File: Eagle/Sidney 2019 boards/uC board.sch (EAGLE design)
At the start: 55 parts, among them J1 39-28-1043

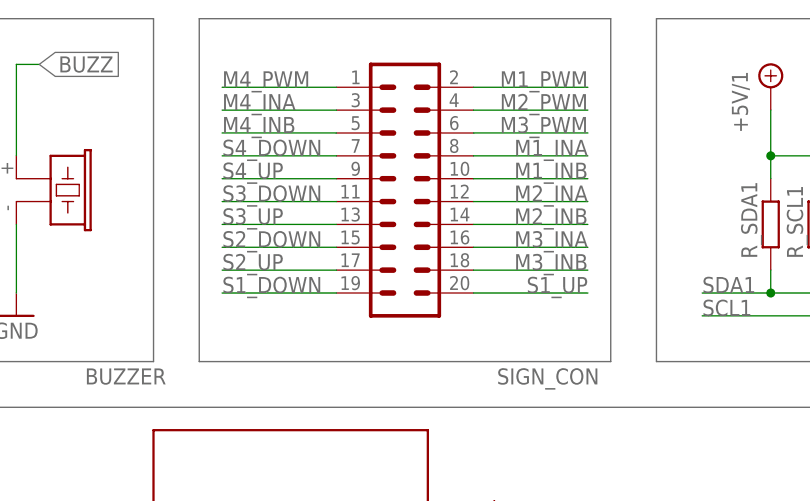
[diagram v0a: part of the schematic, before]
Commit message: Finished components lists for both boards and fixed line sensors' connectors pinout
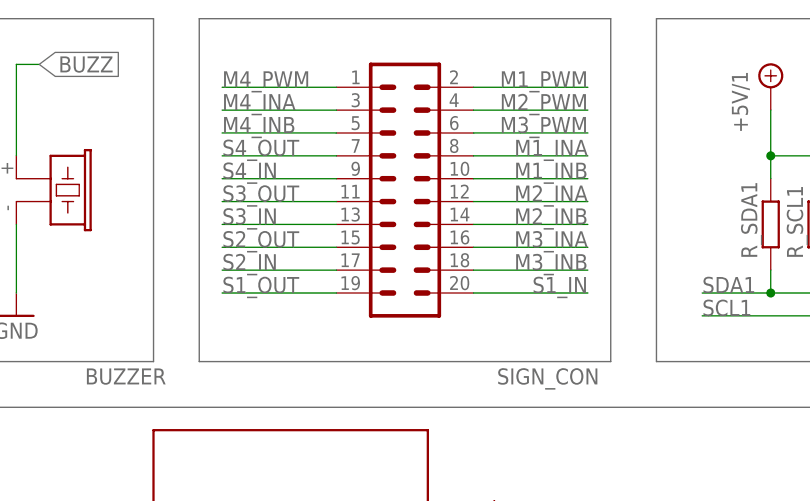
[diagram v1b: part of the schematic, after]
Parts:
- R_SW_DX, R_SW_SX: device rcl:R-EU_R0805 -> rcl:R-EU_R1206
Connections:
- new net S1_IN: SIGN_CON.20
- new net S1_OUT: SIGN_CON.19
- new net S2_IN: SIGN_CON.17
- new net S2_OUT: SIGN_CON.15
- new net S3_IN: SIGN_CON.13
- new net S3_OUT: SIGN_CON.11
- new net S4_IN: SIGN_CON.9
- new net S4_OUT: SIGN_CON.7
- net S1_DOWN: no longer SIGN_CON.19
- net S1_UP: no longer SIGN_CON.20
- net S2_DOWN: no longer SIGN_CON.15
- net S2_UP: no longer SIGN_CON.17
- net S3_DOWN: no longer SIGN_CON.11
- net S3_UP: no longer SIGN_CON.13
- net S4_DOWN: no longer SIGN_CON.7
- net S4_UP: no longer SIGN_CON.9
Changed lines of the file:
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@@
 <part name="SW_SX" library="switch" library_urn="urn:adsk.eagle:library:380" deviceset="TL38PO" device="" package3d_urn="urn:adsk.eagle:package:27745/1"/>
 <part name="GND28" library="supply1" deviceset="GND" device=""/>
-<part name="R_SW_SX" library="rcl" library_urn="urn:adsk.eagle:library:334" deviceset="R-EU_" device="R0805" package3d_urn="urn:adsk.eagle:package:23553/2" value="330"/>
+<part name="R_SW_SX" library="rcl" library_urn="urn:adsk.eagle:library:334" deviceset="R-EU_" device="R1206" package3d_urn="urn:adsk.eagle:package:23540/2" value="330"/>
 <part name="LED_SW_SX" library="SparkFun-LED" deviceset="LED" device="3MM"/>
 <part name="SW_DX" library="switch" library_urn="urn:adsk.eagle:library:380" deviceset="TL38PO" device="" package3d_urn="urn:adsk.eagle:package:27745/1"/>
 <part name="GND38" library="supply1" deviceset="GND" device=""/>
-<part name="R_SW_DX" library="rcl" library_urn="urn:adsk.eagle:library:334" deviceset="R-EU_" device="R0805" package3d_urn="urn:adsk.eagle:package:23553/2" value="330"/>
+<part name="R_SW_DX" library="rcl" library_urn="urn:adsk.eagle:library:334" deviceset="R-EU_" device="R1206" package3d_urn="urn:adsk.eagle:package:23540/2" value="330"/>
 <part name="LED_SW_DX" library="SparkFun-LED" deviceset="LED" device="3MM"/>
 <part name="R_SDA" library="rcl" library_urn="urn:adsk.eagle:library:334" deviceset="R-EU_" device="R0805" package3d_urn="urn:adsk.eagle:package:23553/2" value="3.3k"/>
@@
 <label x="58.42" y="17.78" size="1.778" layer="95"/>
 </segment>
-<segment>
-<pinref part="SIGN_CON" gate="G$1" pin="20"/>
-<wire x1="58.42" y1="104.14" x2="71.12" y2="104.14" width="0.1524" layer="91"/>
-<label x="71.12" y="104.14" size="1.778" layer="95" align="bottom-right"/>
-</segment>
 </net>
 <net name="S1_DOWN" class="0">
@@
 <label x="58.42" y="20.32" size="1.778" layer="95"/>
 </segment>
-<segment>
-<pinref part="SIGN_CON" gate="G$1" pin="19"/>
-<wire x1="43.18" y1="104.14" x2="30.48" y2="104.14" width="0.1524" layer="91"/>
-<label x="30.48" y="104.14" size="1.778" layer="95"/>
-</segment>
 </net>
 <net name="M1_PWM" class="0">
@@
 <label x="58.42" y="22.86" size="1.778" layer="95"/>
 </segment>
-<segment>
-<pinref part="SIGN_CON" gate="G$1" pin="17"/>
-<wire x1="43.18" y1="106.68" x2="30.48" y2="106.68" width="0.1524" layer="91"/>
-<label x="30.48" y="106.68" size="1.778" layer="95"/>
-</segment>
 </net>
 <net name="S2_DOWN" class="0">
@@
 <label x="58.42" y="25.4" size="1.778" layer="95"/>
 </segment>
-<segment>
-<pinref part="SIGN_CON" gate="G$1" pin="15"/>
-<wire x1="43.18" y1="109.22" x2="30.48" y2="109.22" width="0.1524" layer="91"/>
-<label x="30.48" y="109.22" size="1.778" layer="95"/>
-</segment>
 </net>
 <net name="S4_DOWN" class="0">
@@
 <label x="58.42" y="50.8" size="1.778" layer="95"/>
 </segment>
-<segment>
-<pinref part="SIGN_CON" gate="G$1" pin="7"/>
-<wire x1="43.18" y1="119.38" x2="30.48" y2="119.38" width="0.1524" layer="91"/>
-<label x="30.48" y="119.38" size="1.778" layer="95"/>
-</segment>
 </net>
 <net name="S4_UP" class="0">
@@
 <label x="58.42" y="48.26" size="1.778" layer="95"/>
 </segment>
-<segment>
-<pinref part="SIGN_CON" gate="G$1" pin="9"/>
-<wire x1="43.18" y1="116.84" x2="30.48" y2="116.84" width="0.1524" layer="91"/>
-<label x="30.48" y="116.84" size="1.778" layer="95"/>
-</segment>
 </net>
 <net name="S3_UP" class="0">
@@
 <label x="58.42" y="33.02" size="1.778" layer="95"/>
 </segment>
-<segment>
-<pinref part="SIGN_CON" gate="G$1" pin="13"/>
-<wire x1="43.18" y1="111.76" x2="30.48" y2="111.76" width="0.1524" layer="91"/>
-<label x="30.48" y="111.76" size="1.778" layer="95"/>
-</segment>
 </net>
 <net name="S3_DOWN" class="0">
@@
 <wire x1="58.42" y1="45.72" x2="66.04" y2="45.72" width="0.1524" layer="91"/>
 <label x="58.42" y="45.72" size="1.778" layer="95"/>
-</segment>
-<segment>
-<pinref part="SIGN_CON" gate="G$1" pin="11"/>
-<wire x1="43.18" y1="114.3" x2="30.48" y2="114.3" width="0.1524" layer="91"/>
-<label x="30.48" y="114.3" size="1.778" layer="95"/>
 </segment>
 </net>
@@
 </segment>
 </net>
+<net name="S1_IN" class="0">
+<segment>
+<pinref part="SIGN_CON" gate="G$1" pin="20"/>
+<wire x1="58.42" y1="104.14" x2="71.12" y2="104.14" width="0.1524" layer="91"/>
+<label x="71.12" y="104.14" size="1.778" layer="95" align="bottom-right"/>
+</segment>
+</net>
+<net name="S1_OUT" class="0">
+<segment>
+<pinref part="SIGN_CON" gate="G$1" pin="19"/>
+<wire x1="43.18" y1="104.14" x2="30.48" y2="104.14" width="0.1524" layer="91"/>
+<label x="30.48" y="104.14" size="1.778" layer="95"/>
+</segment>
+</net>
+<net name="S2_IN" class="0">
+<segment>
+<pinref part="SIGN_CON" gate="G$1" pin="17"/>
+<wire x1="43.18" y1="106.68" x2="30.48" y2="106.68" width="0.1524" layer="91"/>
+<label x="30.48" y="106.68" size="1.778" layer="95"/>
+</segment>
+</net>
+<net name="S2_OUT" class="0">
+<segment>
+<pinref part="SIGN_CON" gate="G$1" pin="15"/>
+<wire x1="43.18" y1="109.22" x2="30.48" y2="109.22" width="0.1524" layer="91"/>
+<label x="30.48" y="109.22" size="1.778" layer="95"/>
+</segment>
+</net>
+<net name="S3_IN" class="0">
+<segment>
+<pinref part="SIGN_CON" gate="G$1" pin="13"/>
+<wire x1="43.18" y1="111.76" x2="30.48" y2="111.76" width="0.1524" layer="91"/>
+<label x="30.48" y="111.76" size="1.778" layer="95"/>
+</segment>
+</net>
+<net name="S3_OUT" class="0">
+<segment>
+<pinref part="SIGN_CON" gate="G$1" pin="11"/>
+<wire x1="43.18" y1="114.3" x2="30.48" y2="114.3" width="0.1524" layer="91"/>
+<label x="30.48" y="114.3" size="1.778" layer="95"/>
+</segment>
+</net>
+<net name="S4_IN" class="0">
+<segment>
+<pinref part="SIGN_CON" gate="G$1" pin="9"/>
+<wire x1="43.18" y1="116.84" x2="30.48" y2="116.84" width="0.1524" layer="91"/>
+<label x="30.48" y="116.84" size="1.778" layer="95"/>
+</segment>
+</net>
+<net name="S4_OUT" class="0">
+<segment>
+<pinref part="SIGN_CON" gate="G$1" pin="7"/>
+<wire x1="43.18" y1="119.38" x2="30.48" y2="119.38" width="0.1524" layer="91"/>
+<label x="30.48" y="119.38" size="1.778" layer="95"/>
+</segment>
+</net>

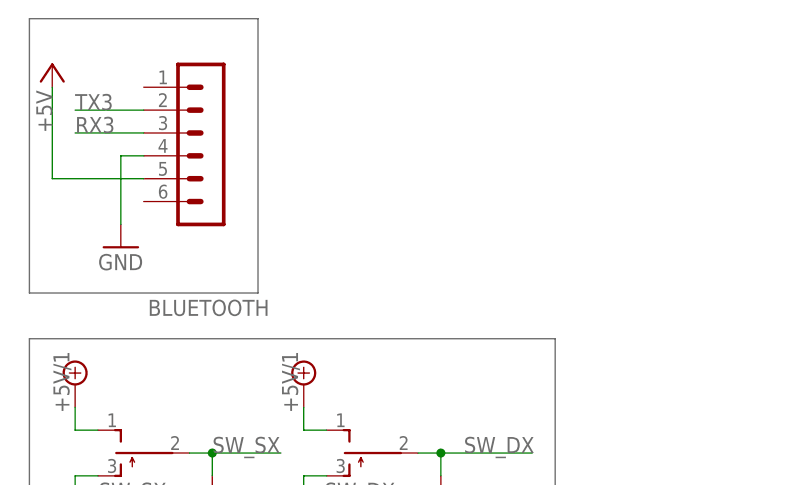
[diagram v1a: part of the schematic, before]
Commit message: Added grove connectors for auxiliary supply
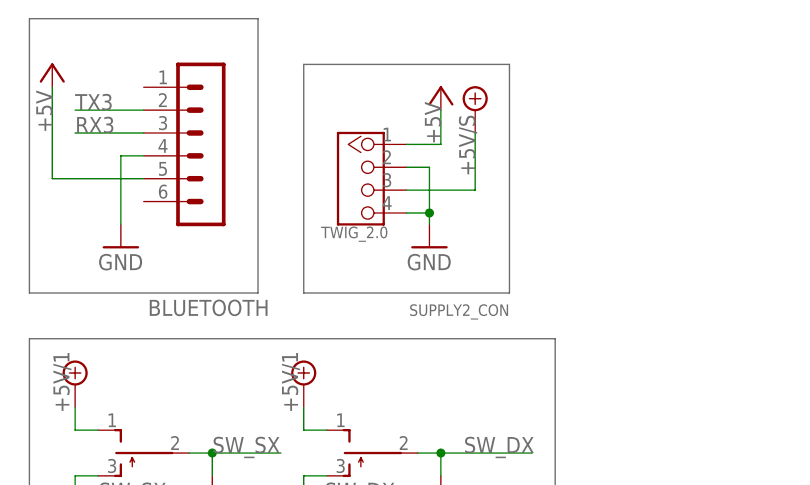
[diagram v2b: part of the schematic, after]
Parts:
- added SUPPLY2_CON: TWIG_2.0, CONNECTER:TWIG_2.0
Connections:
- net +5V: now also SUPPLY2_CON.1
- net +5V/S: now also SUPPLY2_CON.3
- net GND: now also SUPPLY2_CON.2, SUPPLY2_CON.4
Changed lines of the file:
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@@
 <part name="P+16" library="supply1" library_urn="urn:adsk.eagle:library:371" deviceset="+5V" device=""/>
 <part name="SUPPLY4" library="supply2" library_urn="urn:adsk.eagle:library:372" deviceset="+5V/1" device=""/>
+<part name="SUPPLY2_CON" library="CONNECTER" deviceset="TWIG_2.0" device=""/>
+<part name="P+10" library="supply1" library_urn="urn:adsk.eagle:library:371" deviceset="+5V" device=""/>
+<part name="SUPPLY10" library="supply2" library_urn="urn:adsk.eagle:library:372" deviceset="+5V/1" device=""/>
+<part name="GND18" library="supply1" library_urn="urn:adsk.eagle:library:371" deviceset="GND" device=""/>
 </parts>
 <sheets>
@@
 <wire x1="391.16" y1="78.74" x2="424.18" y2="78.74" width="0.1524" layer="95"/>
 <text x="408.94" y="48.26" size="1.778" layer="95">SUPPLY_CON</text>
+<wire x1="358.14" y1="129.54" x2="381" y2="129.54" width="0.1524" layer="95"/>
+<wire x1="381" y1="129.54" x2="381" y2="104.14" width="0.1524" layer="95"/>
+<wire x1="381" y1="104.14" x2="358.14" y2="104.14" width="0.1524" layer="95"/>
+<wire x1="358.14" y1="104.14" x2="358.14" y2="129.54" width="0.1524" layer="95"/>
 </plain>
 <instances>
@@
 </instance>
 <instance part="SUPPLY4" gate="G$1" x="421.64" y="73.66" smashed="yes"/>
+<instance part="SUPPLY2_CON" gate="G$1" x="365.76" y="116.84" smashed="yes" rot="MR0">
+<attribute name="NAME" x="381" y="101.6" size="1.27" layer="95" rot="MR0"/>
+<attribute name="VALUE" x="367.538" y="110.236" size="1.27" layer="96" rot="MR0"/>
+</instance>
+<instance part="P+10" gate="1" x="373.38" y="127" smashed="yes">
+<attribute name="VALUE" x="373.38" y="120.65" size="1.778" layer="96" rot="R90"/>
+</instance>
+<instance part="SUPPLY10" gate="G$1" x="377.19" y="124.46" smashed="yes"/>
+<instance part="GND18" gate="1" x="372.11" y="109.22" smashed="yes">
+<attribute name="VALUE" x="369.57" y="106.68" size="1.778" layer="96"/>
+</instance>
 </instances>
 <busses>
@@
 <wire x1="408.94" y1="58.42" x2="408.94" y2="60.96" width="0.1524" layer="91"/>
 <junction x="408.94" y="60.96"/>
+</segment>
+<segment>
+<pinref part="SUPPLY2_CON" gate="G$1" pin="2"/>
+<pinref part="GND18" gate="1" pin="GND"/>
+<wire x1="369.57" y1="118.11" x2="372.11" y2="118.11" width="0.1524" layer="91"/>
+<wire x1="372.11" y1="118.11" x2="372.11" y2="113.03" width="0.1524" layer="91"/>
+<pinref part="SUPPLY2_CON" gate="G$1" pin="4"/>
+<wire x1="372.11" y1="113.03" x2="372.11" y2="111.76" width="0.1524" layer="91"/>
+<wire x1="369.57" y1="113.03" x2="372.11" y2="113.03" width="0.1524" layer="91"/>
+<junction x="372.11" y="113.03"/>
 </segment>
 </net>
@@
 <wire x1="393.7" y1="73.66" x2="393.7" y2="66.04" width="0.1524" layer="91"/>
 </segment>
+<segment>
+<pinref part="P+10" gate="1" pin="+5V"/>
+<wire x1="373.38" y1="124.46" x2="373.38" y2="120.65" width="0.1524" layer="91"/>
+<pinref part="SUPPLY2_CON" gate="G$1" pin="1"/>
+<wire x1="373.38" y1="120.65" x2="369.57" y2="120.65" width="0.1524" layer="91"/>
+</segment>
 </net>
 <net name="TX3" class="0">
@@
 <label x="421.64" y="68.58" size="1.778" layer="95" rot="R90"/>
 </segment>
-</net>
+<segment>
+<pinref part="SUPPLY10" gate="G$1" pin="+5V/1"/>
+<pinref part="SUPPLY2_CON" gate="G$1" pin="3"/>
+<wire x1="377.19" y1="121.92" x2="377.19" y2="115.57" width="0.1524" layer="91"/>
+<wire x1="377.19" y1="115.57" x2="369.57" y2="115.57" width="0.1524" layer="91"/>
+<label x="377.19" y="117.094" size="1.778" layer="95" rot="R90"/>
+</segment>
+</net>
